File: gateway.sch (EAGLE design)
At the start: 40 parts

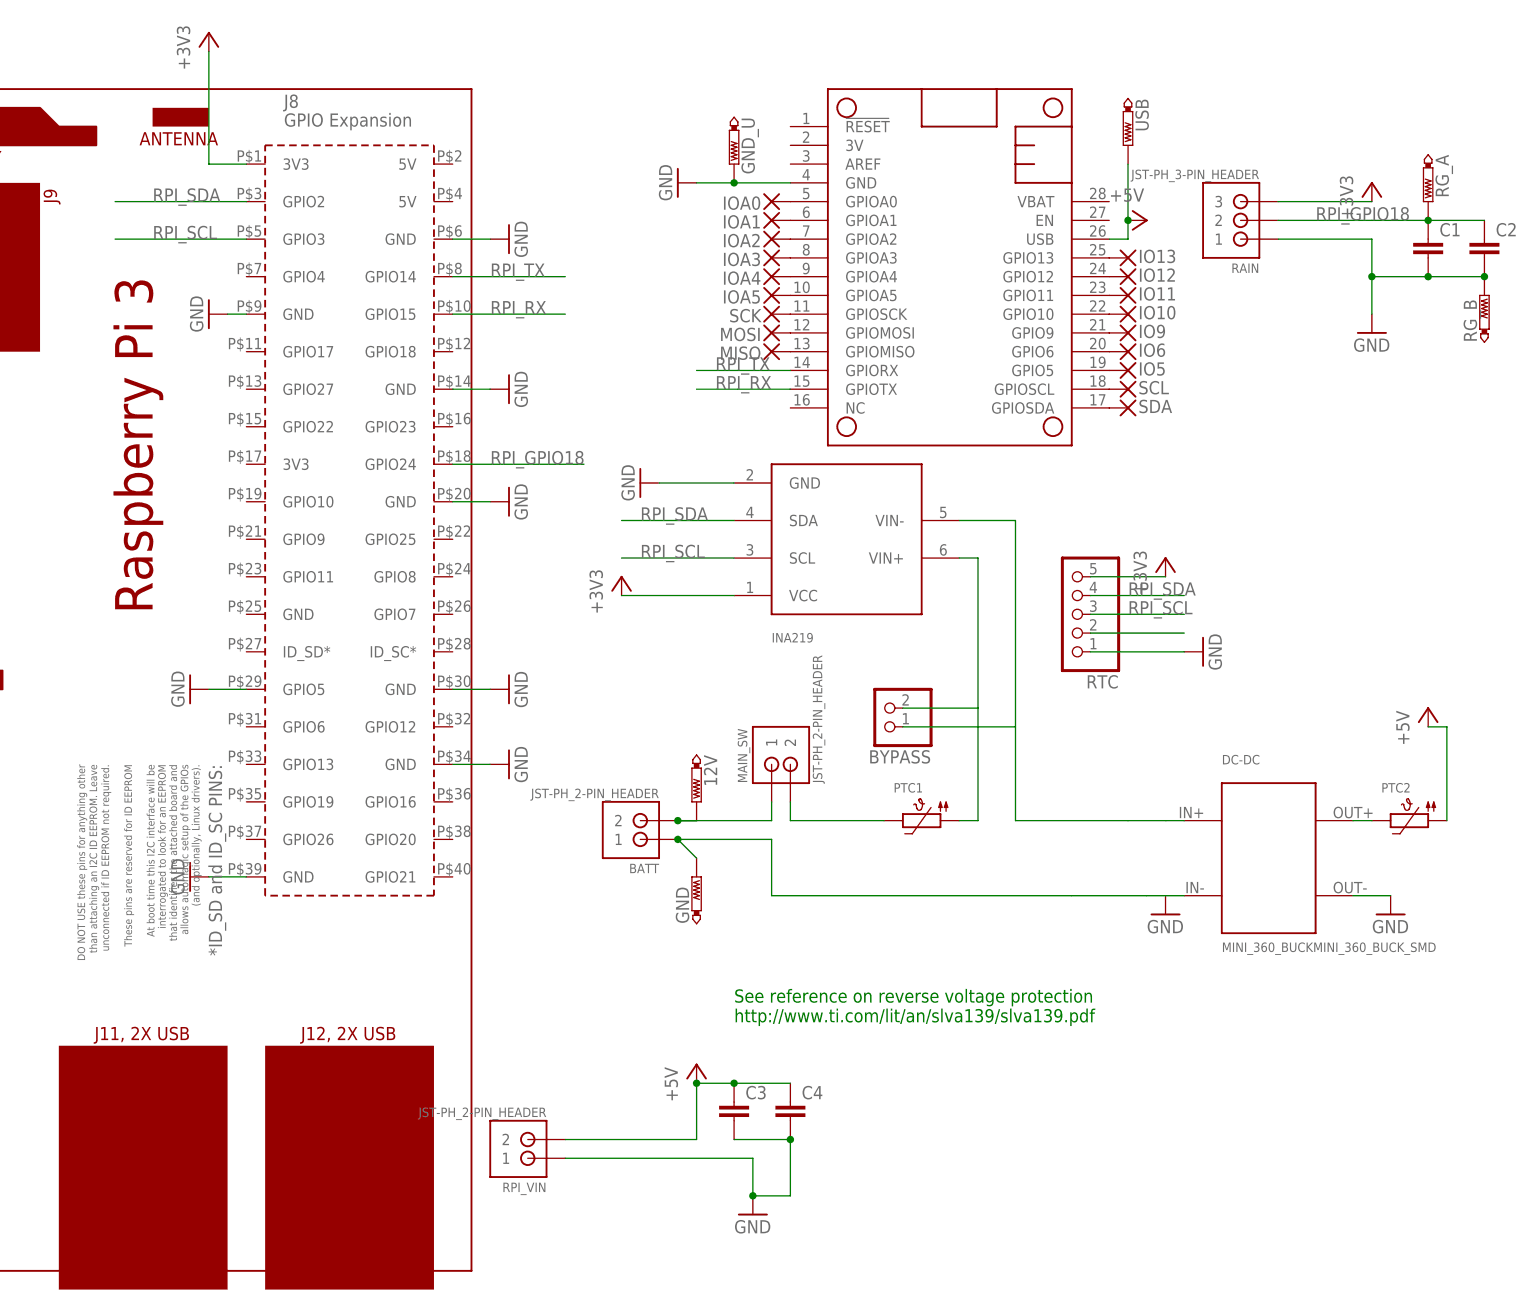
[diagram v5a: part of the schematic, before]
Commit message: new gateway versions
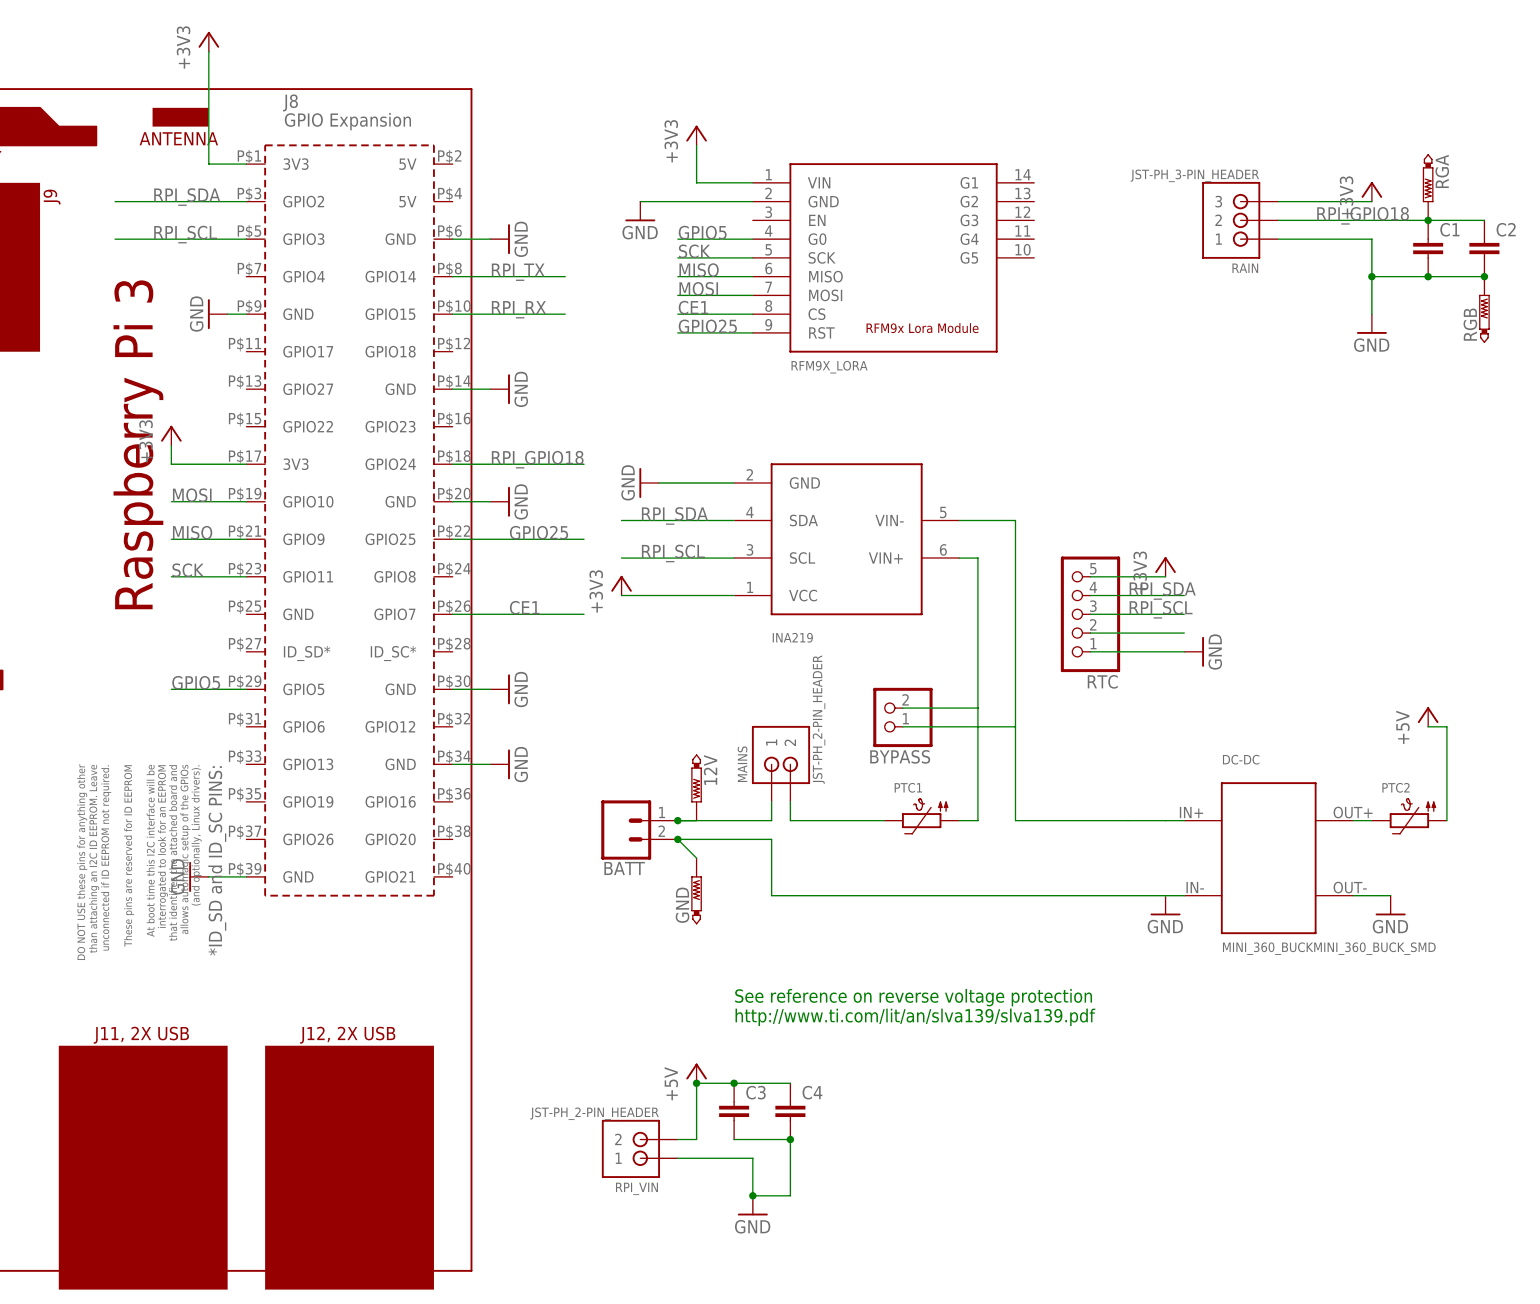
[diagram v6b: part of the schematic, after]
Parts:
- removed GND_U, USB: PTR1PAD1-13, testpad:PTR1PAD1-13
- removed IO10, IO11, IO12, IO13, IO5, IO6, IO9, IOA0, IOA1, IOA2, IOA3, IOA4, IOA5, MISO, MOSI, SCK, SCL, SDA: (no value), wirepad:SMD2
- removed MS2: FEATHERWINGFEATHERWING_EDC, adafruit:FEATHERWINGFEATHERWING_EDC
- added RFM9X_LORA: RFM9X_MODULE, edc_modules:RFM9X_MODULE
- BATT: value JST-PH_2-PIN_HEADER -> (none); device SRG:JST-PH_2-PIN_HEADER -> SparkFun-Connectors:CONN_02POLAR
- renumbered MAIN_SW to MAINS, RG_A to RGA, RG_B to RGB
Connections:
- removed net N$1: MS2.GPIOSDA, SDA.P
- removed net N$10: IO9.P, MS2.GPIO9
- removed net N$11: IO10.P, MS2.GPIO10
- removed net N$12: IO11.P, MS2.GPIO11
- removed net N$13: IO12.P, MS2.GPIO12
- removed net N$14: IO13.P, MS2.GPIO13
- removed net N$15: MISO.P, MS2.GPIOMISO
- removed net N$16: MOSI.P, MS2.GPIOMOSI
- removed net N$17: MS2.GPIOSCK, SCK.P
- removed net N$18: IOA5.P, MS2.GPIOA5
- removed net N$19: IOA4.P, MS2.GPIOA4
- removed net N$20: IOA3.P, MS2.GPIOA3
- removed net N$21: IOA2.P, MS2.GPIOA2
- removed net N$22: IOA1.P, MS2.GPIOA1
- removed net N$23: IOA0.P, MS2.GPIOA0
- removed net N$7: MS2.GPIOSCL, SCL.P
- removed net N$8: IO5.P, MS2.GPIO5
- removed net N$9: IO6.P, MS2.GPIO6
- new net CE1: PCB2.GPIO7, RFM9X_LORA.CS
- new net GPIO25: PCB2.GPIO25, RFM9X_LORA.RST
- new net GPIO5: PCB2.GPIO5, RFM9X_LORA.G0
- new net MISO: PCB2.GPIO9, RFM9X_LORA.MISO
- new net MOSI: PCB2.GPIO10, RFM9X_LORA.MOSI
- new net SCK: PCB2.GPIO11, RFM9X_LORA.SCK
- net +3V3: now also PCB2.3V3@17, RFM9X_LORA.VIN
- net +5V: no longer MS2.USB, USB.TP
- net GND: now also BATT.2, RFM9X_LORA.GND; no longer BATT.1, GND_U.TP, MS2.GND, PCB2.GPIO5
- net N$2: now also BATT.1; no longer BATT.2
- net RPI_RX: no longer MS2.GPIOTX
- net RPI_TX: no longer MS2.GPIORX
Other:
- moved on the sheet: RPI_VIN

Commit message: few gateway revisions
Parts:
- added ALARM: JST-PH_3-PIN_HEADER, SRG:JST-PH_3-PIN_HEADER
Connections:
- new net ALARM_TRIG: ALARM.2, PCB2.GPIO4
- net +5V: now also ALARM.3
- net GND: now also ALARM.1
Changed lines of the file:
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@@
 <part name="+3V6" library="supply1" library_urn="urn:adsk.eagle:library:371" deviceset="+3V3" device=""/>
 <part name="BATT" library="SparkFun-Connectors" deviceset="CONN_02" device="POLAR"/>
+<part name="ALARM" library="SRG" deviceset="JST-PH_3-PIN_HEADER" device=""/>
+<part name="GND12" library="supply1" library_urn="urn:adsk.eagle:library:371" deviceset="GND" device=""/>
+<part name="P+3" library="supply1" library_urn="urn:adsk.eagle:library:371" deviceset="+5V" device=""/>
 </parts>
 <sheets>
@@
 <instance part="+3V6" gate="G$1" x="71.12" y="121.92"/>
 <instance part="BATT" gate="G$1" x="132.08" y="68.58" rot="MR180"/>
+<instance part="ALARM" gate="G$1" x="215.9" y="121.92" rot="R180"/>
+<instance part="GND12" gate="1" x="226.06" y="114.3"/>
+<instance part="P+3" gate="1" x="226.06" y="129.54"/>
 </instances>
 <busses>
@@
 <wire x1="149.86" y1="152.4" x2="134.62" y2="152.4" width="0.1524" layer="91"/>
 </segment>
+<segment>
+<pinref part="ALARM" gate="G$1" pin="1"/>
+<wire x1="220.98" y1="119.38" x2="226.06" y2="119.38" width="0.1524" layer="91"/>
+<wire x1="226.06" y1="119.38" x2="226.06" y2="116.84" width="0.1524" layer="91"/>
+<pinref part="GND12" gate="1" pin="GND"/>
+</segment>
 </net>
 <net name="N$5" class="0">
@@
 <pinref part="PTC2" gate="G$1" pin="1"/>
 </segment>
+<segment>
+<pinref part="ALARM" gate="G$1" pin="3"/>
+<wire x1="220.98" y1="124.46" x2="226.06" y2="124.46" width="0.1524" layer="91"/>
+<wire x1="226.06" y1="124.46" x2="226.06" y2="127" width="0.1524" layer="91"/>
+<pinref part="P+3" gate="1" pin="+5V"/>
+</segment>
 </net>
 <net name="N$6" class="0">
@@
 </segment>
 </net>
+<net name="ALARM_TRIG" class="0">
+<segment>
+<pinref part="PCB2" gate="G$1" pin="GPIO4"/>
+<wire x1="81.28" y1="142.24" x2="63.5" y2="142.24" width="0.1524" layer="91"/>
+<label x="63.5" y="142.24" size="1.778" layer="95"/>
+</segment>
+<segment>
+<pinref part="ALARM" gate="G$1" pin="2"/>
+<wire x1="220.98" y1="121.92" x2="238.76" y2="121.92" width="0.1524" layer="91"/>
+<label x="223.52" y="121.92" size="1.778" layer="95"/>
+</segment>
+</net>
